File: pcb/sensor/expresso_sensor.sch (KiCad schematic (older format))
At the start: 13 parts, among them P1 CONN_2, P2 CONN_2, U1 TAOS_TSL1406R, U2 TAOS_TSL1406R, U3 TAOS_TSL1406R, U4 TAOS_TSL1406R, U5 TAOS_TSL1406R, U6 MAPLE_MINI

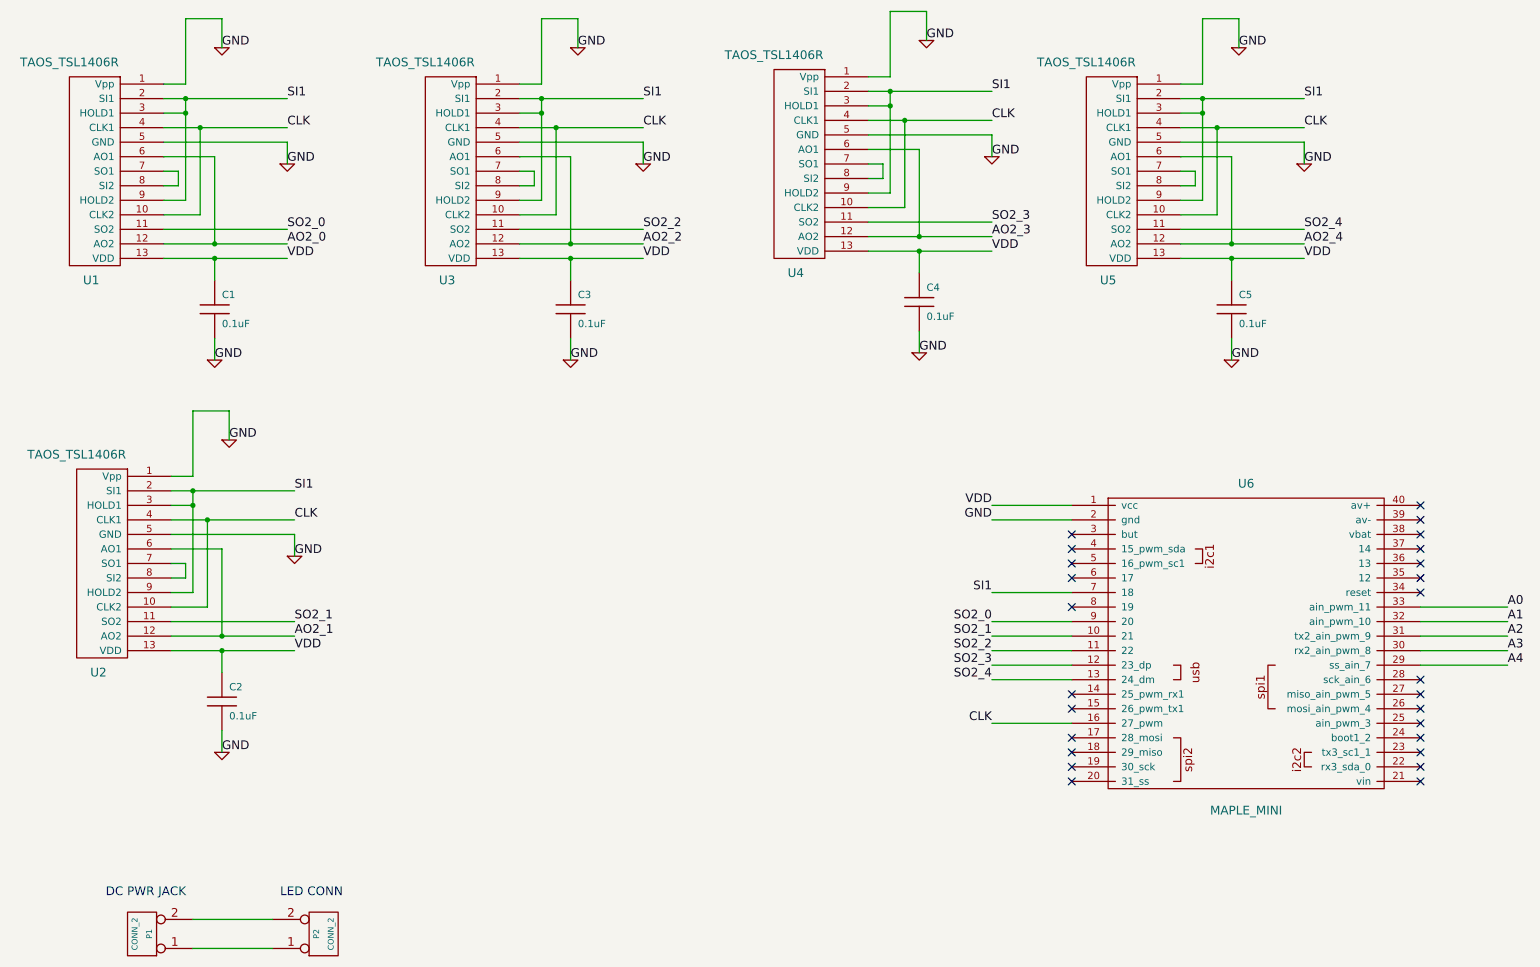
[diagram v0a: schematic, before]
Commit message: Major refactoring of the code for the enclosure.  Finished layout of the PCBs
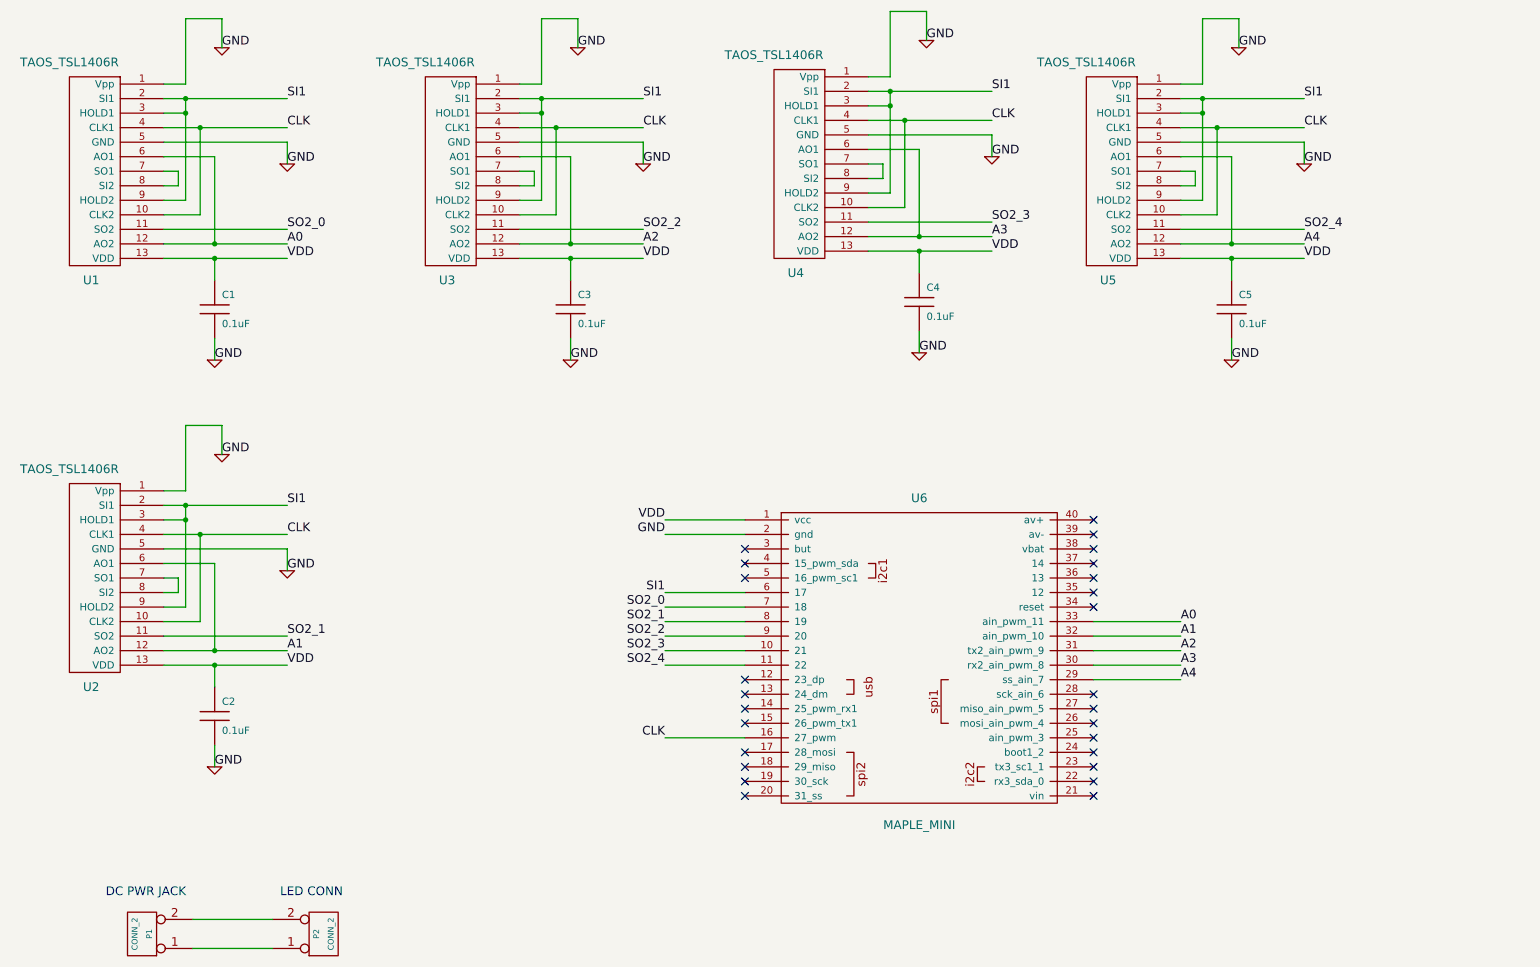
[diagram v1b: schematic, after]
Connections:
- net AO2_0 is gone; now on net A0: U1.12 (AO2), U1.6 (AO1)
- net AO2_1 is gone; now on net A1: U2.12 (AO2), U2.6 (AO1)
- net AO2_2 is gone; now on net A2: U3.12 (AO2), U3.6 (AO1)
- net AO2_3 is gone; now on net A3: U4.12 (AO2), U4.6 (AO1)
- net AO2_4 is gone; now on net A4: U5.12 (AO2), U5.6 (AO1)
- net SI1: now also U6.6 (17); no longer U6.7 (18)
- net SO2_0: now also U6.7 (18); no longer U6.9 (20)
- net SO2_1: now also U6.8 (19); no longer U6.10 (21)
- net SO2_2: now also U6.9 (20); no longer U6.11 (22)
- net SO2_3: now also U6.10 (21); no longer U6.12 (23_dp)
- net SO2_4: now also U6.11 (22); no longer U6.13 (24_dm)
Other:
- moved on the sheet: U6

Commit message: generated gerbers and finalized BOM
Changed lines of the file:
@@
-EESchema Schematic File Version 2  date Mon 17 Sep 2012 09:35:10 AM PDT
+EESchema Schematic File Version 2  date Fri 21 Sep 2012 01:45:22 PM PDT
 LIBS:power
 LIBS:device
@@
 $EndComp
 $Comp
-L GND #PWR?
+L GND #PWR01
 U 1 1 50575057
 P 2100 5750
-F 0 "#PWR?" H 2100 5750 30  0001 C CNN
+F 0 "#PWR01" H 2100 5750 30  0001 C CNN
 F 1 "GND" H 2100 5680 30  0001 C CNN
 	1    2100 5750
@@
 VDD
 $Comp
-L GND #PWR?
+L GND #PWR02
 U 1 1 50575056
 P 2150 3600
-F 0 "#PWR?" H 2150 3600 30  0001 C CNN
+F 0 "#PWR02" H 2150 3600 30  0001 C CNN
 F 1 "GND" H 2150 3530 30  0001 C CNN
 	1    2150 3600
@@
 GND
 $Comp
-L GND #PWR?
+L GND #PWR03
 U 1 1 50575055
 P 2600 4400
-F 0 "#PWR?" H 2600 4400 30  0001 C CNN
+F 0 "#PWR03" H 2600 4400 30  0001 C CNN
 F 1 "GND" H 2600 4330 30  0001 C CNN
 	1    2600 4400
@@
 Connection ~ 2100 5050
 Wire Wire Line
-	2100 5050 2100 5200
-Wire Wire Line
-	2000 4150 1750 4150
-Wire Wire Line
-	2600 4150 2000 4150
-Wire Wire Line
-	2100 4950 2600 4950
-Wire Wire Line
-	1750 4950 2100 4950
-Wire Wire Line
-	2100 4350 1750 4350
+	2100 5200 2100 5050
+Wire Wire Line
+	1750 4150 2600 4150
+Wire Wire Line
+	2600 4950 1750 4950
+Wire Wire Line
+	1750 4350 2100 4350
 Connection ~ 2000 4150
 Wire Wire Line
-	2000 4750 2000 4150
-Wire Wire Line
-	1750 4750 2000 4750
+	2000 4150 2000 4750
+Wire Wire Line
+	2000 4750 1750 4750
 Connection ~ 1900 4050
 Wire Wire Line
-	1900 4050 1900 3950
-Wire Wire Line
-	1900 4650 1900 4050
-Wire Wire Line
-	1750 4650 1900 4650
-Wire Wire Line
-	2150 3400 2150 3600
-Wire Wire Line
-	1900 3400 2150 3400
-Wire Wire Line
-	1900 3850 1900 3400
-Wire Wire Line
-	1750 3850 1900 3850
-Wire Wire Line
-	2100 5050 1750 5050
-Wire Wire Line
-	2600 5050 2100 5050
+	1900 3950 1900 4650
+Wire Wire Line
+	1900 4650 1750 4650
+Wire Wire Line
+	2150 3600 2150 3400
+Wire Wire Line
+	2150 3400 1900 3400
+Wire Wire Line
+	1900 3400 1900 3850
+Wire Wire Line
+	1900 3850 1750 3850
+Wire Wire Line
+	1750 5050 2600 5050
 Wire Wire Line
 	1900 4050 1750 4050
 Connection ~ 1900 3950
 Wire Wire Line
-	2600 4250 1750 4250
-Wire Wire Line
-	2600 4400 2600 4250
-Wire Wire Line
-	1900 3950 1750 3950
-Wire Wire Line
-	2600 3950 1900 3950
-Wire Wire Line
-	2100 4950 2100 4350
+	1750 4250 2600 4250
+Wire Wire Line
+	2600 4250 2600 4400
+Wire Wire Line
+	1750 3950 2600 3950
+Wire Wire Line
+	2100 4350 2100 4950
 Connection ~ 2100 4950
 Wire Wire Line
 	2100 5600 2100 5750
 Wire Wire Line
-	1850 4450 1750 4450
-Wire Wire Line
-	1850 4550 1850 4450
-Wire Wire Line
-	1750 4550 1850 4550
+	1750 4450 1850 4450
+Wire Wire Line
+	1850 4450 1850 4550
+Wire Wire Line
+	1850 4550 1750 4550
 Text Label 5200 5050 2    60   ~ 0
 SO2_4
@@
 Connection ~ 9100 2250
 Wire Wire Line
-	9100 2250 9100 2400
-Wire Wire Line
-	9600 1350 9000 1350
-Wire Wire Line
-	9000 1350 8750 1350
-Wire Wire Line
-	8750 2150 9100 2150
-Wire Wire Line
-	9100 2150 9600 2150
+	9100 2400 9100 2250
+Wire Wire Line
+	9600 1350 8750 1350
+Wire Wire Line
+	8750 2150 9600 2150
 Wire Wire Line
 	8750 1550 9100 1550
@@
 Connection ~ 8900 1250
 Wire Wire Line
-	8900 1150 8900 1250
-Wire Wire Line
-	8900 1250 8900 1850
+	8900 1150 8900 1850
 Wire Wire Line
 	8900 1850 8750 1850
@@
 	8900 1050 8750 1050
 Wire Wire Line
-	9600 2250 9100 2250
-Wire Wire Line
-	9100 2250 8750 2250
+	9600 2250 8750 2250
 Wire Wire Line
 	8900 1250 8750 1250
@@
 	9600 1450 9600 1600
 Wire Wire Line
-	9600 1150 8900 1150
-Wire Wire Line
-	8900 1150 8750 1150
+	9600 1150 8750 1150
 Wire Wire Line
 	9100 1550 9100 2150
@@
 Connection ~ 4550 2250
 Wire Wire Line
-	4550 2250 4550 2400
-Wire Wire Line
-	5050 1350 4450 1350
-Wire Wire Line
-	4450 1350 4200 1350
-Wire Wire Line
-	4200 2150 4550 2150
-Wire Wire Line
-	4550 2150 5050 2150
+	4550 2400 4550 2250
+Wire Wire Line
+	5050 1350 4200 1350
+Wire Wire Line
+	4200 2150 5050 2150
 Wire Wire Line
 	4200 1550 4550 1550
@@
 Connection ~ 4350 1250
 Wire Wire Line
-	4350 1150 4350 1250
-Wire Wire Line
-	4350 1250 4350 1850
+	4350 1150 4350 1850
 Wire Wire Line
 	4350 1850 4200 1850
@@
 	4350 1050 4200 1050
 Wire Wire Line
-	5050 2250 4550 2250
-Wire Wire Line
-	4550 2250 4200 2250
+	5050 2250 4200 2250
 Wire Wire Line
 	4350 1250 4200 1250
@@
 	5050 1450 5050 1600
 Wire Wire Line
-	5050 1150 4350 1150
-Wire Wire Line
-	4350 1150 4200 1150
+	5050 1150 4200 1150
 Wire Wire Line
 	4550 1550 4550 2150
@@
 	6950 2100 6950 1500
 Wire Wire Line
-	7450 1100 6750 1100
-Wire Wire Line
-	6750 1100 6600 1100
+	7450 1100 6600 1100
 Wire Wire Line
 	7450 1550 7450 1400
@@
 Connection ~ 6750 1100
 Wire Wire Line
-	6750 1200 6600 1200
-Wire Wire Line
-	7450 2200 6950 2200
-Wire Wire Line
-	6950 2200 6600 2200
+	6600 1200 6750 1200
+Wire Wire Line
+	7450 2200 6600 2200
 Wire Wire Line
 	6600 1000 6750 1000
@@
 	6600 1800 6750 1800
 Wire Wire Line
-	6750 1800 6750 1200
-Wire Wire Line
-	6750 1200 6750 1100
+	6750 1800 6750 1100
 Connection ~ 6750 1200
 Wire Wire Line
@@
 	6950 1500 6600 1500
 Wire Wire Line
-	6600 2100 6950 2100
-Wire Wire Line
-	6950 2100 7450 2100
-Wire Wire Line
-	7450 1300 6850 1300
-Wire Wire Line
-	6850 1300 6600 1300
+	6600 2100 7450 2100
+Wire Wire Line
+	7450 1300 6600 1300
 Wire Wire Line
 	6950 2200 6950 2350
@@
 	2100 2150 2100 1550
 Wire Wire Line
-	2600 1150 1900 1150
-Wire Wire Line
-	1900 1150 1750 1150
+	2600 1150 1750 1150
 Wire Wire Line
 	2600 1600 2600 1450
@@
 Connection ~ 1900 1150
 Wire Wire Line
-	1900 1250 1750 1250
+	1750 1250 1900 1250
 Wire Wire Line
 	5750 4550 5200 4550
@@
 	5750 4050 5200 4050
 Wire Wire Line
-	2600 2250 2100 2250
-Wire Wire Line
-	2100 2250 1750 2250
+	2600 2250 1750 2250
 Wire Wire Line
 	2500 6800 1950 6800
@@
 	1750 1850 1900 1850
 Wire Wire Line
-	1900 1850 1900 1250
-Wire Wire Line
-	1900 1250 1900 1150
+	1900 1850 1900 1150
 Connection ~ 1900 1250
 Wire Wire Line
@@
 	2100 1550 1750 1550
 Wire Wire Line
-	1750 2150 2100 2150
-Wire Wire Line
-	2100 2150 2600 2150
-Wire Wire Line
-	2600 1350 2000 1350
-Wire Wire Line
-	2000 1350 1750 1350
+	1750 2150 2600 2150
+Wire Wire Line
+	2600 1350 1750 1350
 Wire Wire Line
 	2100 2250 2100 2400
@@
 $EndComp
 $Comp
-L GND #PWR01
+L GND #PWR04
 U 1 1 4F36C830
 P 9100 2950
-F 0 "#PWR01" H 9100 2950 30  0001 C CNN
+F 0 "#PWR04" H 9100 2950 30  0001 C CNN
 F 1 "GND" H 9100 2880 30  0001 C CNN
 	1    9100 2950
@@
 VDD
 $Comp
-L GND #PWR02
+L GND #PWR05
 U 1 1 4F36C82F
 P 9150 800
-F 0 "#PWR02" H 9150 800 30  0001 C CNN
+F 0 "#PWR05" H 9150 800 30  0001 C CNN
 F 1 "GND" H 9150 730 30  0001 C CNN
 	1    9150 800
@@
 GND
 $Comp
-L GND #PWR03
+L GND #PWR06
 U 1 1 4F36C82E
 P 9600 1600
-F 0 "#PWR03" H 9600 1600 30  0001 C CNN
+F 0 "#PWR06" H 9600 1600 30  0001 C CNN
 F 1 "GND" H 9600 1530 30  0001 C CNN
 	1    9600 1600
@@
 $EndComp
 $Comp
-L GND #PWR04
+L GND #PWR07
 U 1 1 4F36C825
 P 4550 2950
-F 0 "#PWR04" H 4550 2950 30  0001 C CNN
+F 0 "#PWR07" H 4550 2950 30  0001 C CNN
 F 1 "GND" H 4550 2880 30  0001 C CNN
 	1    4550 2950
@@
 VDD
 $Comp
-L GND #PWR05
+L GND #PWR08
 U 1 1 4F36C824
 P 4600 800
-F 0 "#PWR05" H 4600 800 30  0001 C CNN
+F 0 "#PWR08" H 4600 800 30  0001 C CNN
 F 1 "GND" H 4600 730 30  0001 C CNN
 	1    4600 800
@@
 GND
 $Comp
-L GND #PWR06
+L GND #PWR09
 U 1 1 4F36C823
 P 5050 1600
-F 0 "#PWR06" H 5050 1600 30  0001 C CNN
+F 0 "#PWR09" H 5050 1600 30  0001 C CNN
 F 1 "GND" H 5050 1530 30  0001 C CNN
 	1    5050 1600
@@
 GND
 $Comp
-L GND #PWR07
+L GND #PWR010
 U 1 1 4F36C822
 P 7450 1550
-F 0 "#PWR07" H 7450 1550 30  0001 C CNN
+F 0 "#PWR010" H 7450 1550 30  0001 C CNN
 F 1 "GND" H 7450 1480 30  0001 C CNN
 	1    7450 1550
@@
 GND
 $Comp
-L GND #PWR08
+L GND #PWR011
 U 1 1 4F36C821
 P 7000 750
-F 0 "#PWR08" H 7000 750 30  0001 C CNN
+F 0 "#PWR011" H 7000 750 30  0001 C CNN
 F 1 "GND" H 7000 680 30  0001 C CNN
 	1    7000 750
@@
 GND
 $Comp
-L GND #PWR09
+L GND #PWR012
 U 1 1 4F36C820
 P 6950 2900
-F 0 "#PWR09" H 6950 2900 30  0001 C CNN
+F 0 "#PWR012" H 6950 2900 30  0001 C CNN
 F 1 "GND" H 6950 2830 30  0001 C CNN
 	1    6950 2900

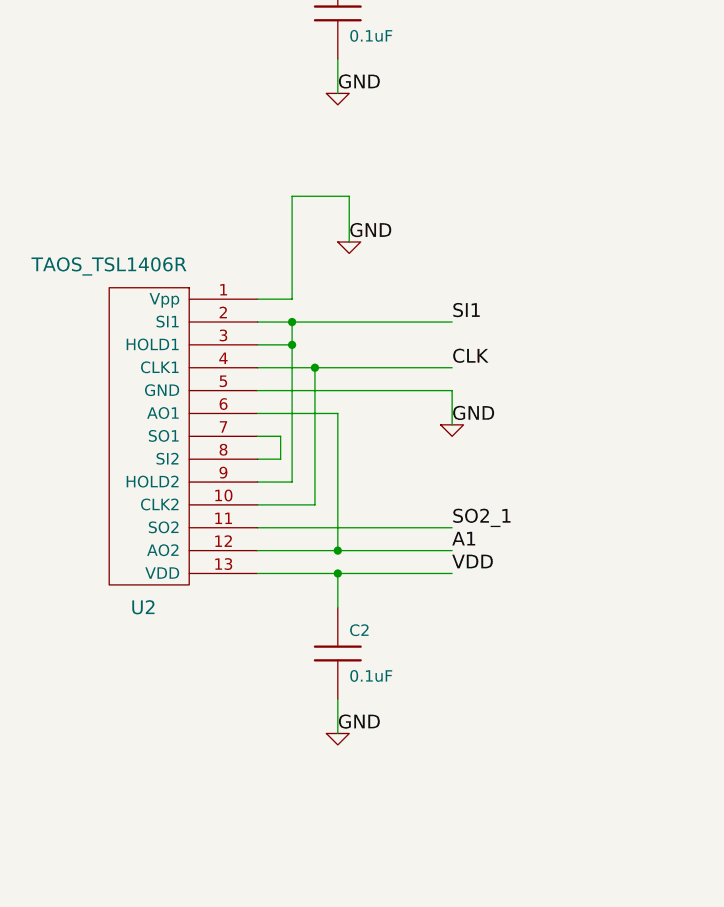
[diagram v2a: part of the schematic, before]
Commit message: Redesigned sensor pcb, and modified enclosure accordingly.
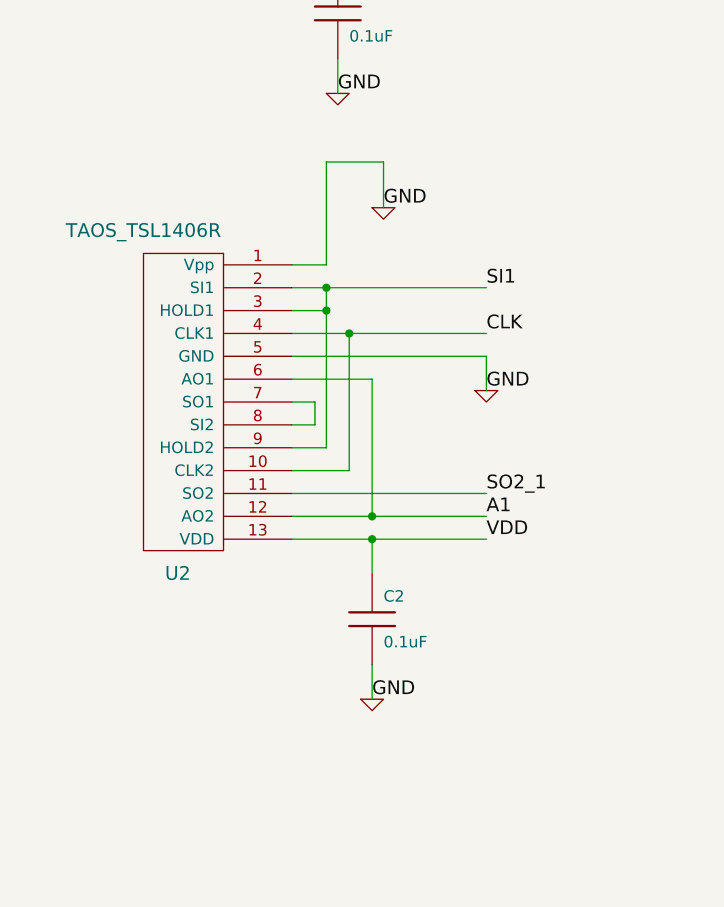
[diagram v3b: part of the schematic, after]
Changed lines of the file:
@@
-EESchema Schematic File Version 2  date Fri 21 Sep 2012 01:45:22 PM PDT
+EESchema Schematic File Version 2  date Thu 11 Oct 2012 06:36:20 PM PDT
 LIBS:power
 LIBS:device
@@
 Sheet 1 1
 Title ""
-Date "17 sep 2012"
+Date "12 oct 2012"
 Rev ""
 Comp ""
@@
 Comment4 ""
 $EndDescr
-NoConn ~ 5750 5250
-NoConn ~ 5750 5150
 $Comp
 L TAOS_TSL1406R U2
-U 1 1 50575059
-P 1450 4450
-F 0 "U2" H 1650 3700 60  0000 C CNN
-F 1 "TAOS_TSL1406R" H 1800 5200 60  0000 C CNN
-	1    1450 4450
+U 1 1 5077711F
+P 1600 4300
+F 0 "U2" H 1800 3550 60  0000 C CNN
+F 1 "TAOS_TSL1406R" H 1950 5050 60  0000 C CNN
+	1    1600 4300
 	-1   0    0    -1
 $EndComp
 $Comp
 L C C2
-U 1 1 50575058
-P 2100 5400
-F 0 "C2" H 2150 5500 50  0000 L CNN
-F 1 "0.1uF" H 2150 5300 50  0000 L CNN
-	1    2100 5400
+U 1 1 5077711E
+P 2250 5250
+F 0 "C2" H 2300 5350 50  0000 L CNN
+F 1 "0.1uF" H 2300 5150 50  0000 L CNN
+	1    2250 5250
 	1    0    0    -1
 $EndComp
 $Comp
-L GND #PWR01
-U 1 1 50575057
-P 2100 5750
-F 0 "#PWR01" H 2100 5750 30  0001 C CNN
-F 1 "GND" H 2100 5680 30  0001 C CNN
-	1    2100 5750
+L GND #PWR?
+U 1 1 5077711D
+P 2250 5600
+F 0 "#PWR?" H 2250 5600 30  0001 C CNN
+F 1 "GND" H 2250 5530 30  0001 C CNN
+	1    2250 5600
 	1    0    0    -1
 $EndComp
-Text Label 2100 5750 0    60   ~ 0
+Text Label 2250 5600 0    60   ~ 0
 GND
-Text Label 2600 5050 0    60   ~ 0
+Text Label 2750 4900 0    60   ~ 0
 VDD
 $Comp
-L GND #PWR02
-U 1 1 50575056
-P 2150 3600
-F 0 "#PWR02" H 2150 3600 30  0001 C CNN
-F 1 "GND" H 2150 3530 30  0001 C CNN
-	1    2150 3600
+L GND #PWR?
+U 1 1 5077711C
+P 2300 3450
+F 0 "#PWR?" H 2300 3450 30  0001 C CNN
+F 1 "GND" H 2300 3380 30  0001 C CNN
+	1    2300 3450
 	1    0    0    -1
 $EndComp
-Text Label 2150 3600 0    60   ~ 0
+Text Label 2300 3450 0    60   ~ 0
 GND
 $Comp
-L GND #PWR03
-U 1 1 50575055
-P 2600 4400
-F 0 "#PWR03" H 2600 4400 30  0001 C CNN
-F 1 "GND" H 2600 4330 30  0001 C CNN
-	1    2600 4400
+L GND #PWR?
+U 1 1 5077711B
+P 2750 4250
+F 0 "#PWR?" H 2750 4250 30  0001 C CNN
+F 1 "GND" H 2750 4180 30  0001 C CNN
+	1    2750 4250
 	1    0    0    -1
 $EndComp
-Text Label 2600 4400 0    60   ~ 0
+Text Label 2750 4250 0    60   ~ 0
 GND
-Text Label 2600 3950 0    60   ~ 0
+Text Label 2750 3800 0    60   ~ 0
 SI1
-Text Label 2600 4150 0    60   ~ 0
+Text Label 2750 4000 0    60   ~ 0
 CLK
-Text Label 2600 4850 0    60   ~ 0
+Text Label 2750 4700 0    60   ~ 0
 SO2_1
-Text Label 2600 4950 0    60   ~ 0
+Text Label 2750 4800 0    60   ~ 0
 A1
 Wire Wire Line
-	1750 4850 2600 4850
-Connection ~ 2100 5050
+	1900 4700 2750 4700
+Connection ~ 2250 4900
 Wire Wire Line
-	2100 5200 2100 5050
+	2250 4900 2250 5050
 Wire Wire Line
-	1750 4150 2600 4150
+	2750 4000 1900 4000
 Wire Wire Line
-	2600 4950 1750 4950
+	1900 4800 2750 4800
 Wire Wire Line
-	1750 4350 2100 4350
-Connection ~ 2000 4150
+	2250 4200 1900 4200
+Connection ~ 2150 4000
 Wire Wire Line
-	2000 4150 2000 4750
+	2150 4600 2150 4000
 Wire Wire Line
-	2000 4750 1750 4750
-Connection ~ 1900 4050
+	1900 4600 2150 4600
+Connection ~ 2050 3900
 Wire Wire Line
-	1900 3950 1900 4650
+	2050 4500 2050 3800
 Wire Wire Line
-	1900 4650 1750 4650
+	1900 4500 2050 4500
 Wire Wire Line
-	2150 3600 2150 3400
+	2300 3250 2300 3450
 Wire Wire Line
-	2150 3400 1900 3400
+	2050 3250 2300 3250
 Wire Wire Line
-	1900 3400 1900 3850
+	2050 3700 2050 3250
 Wire Wire Line
-	1900 3850 1750 3850
+	1900 3700 2050 3700
 Wire Wire Line
-	1750 5050 2600 5050
+	2750 4900 1900 4900
 Wire Wire Line
-	1900 4050 1750 4050
-Connection ~ 1900 3950
+	1900 3900 2050 3900
+Connection ~ 2050 3800
 Wire Wire Line
-	1750 4250 2600 4250
+	2750 4100 1900 4100
 Wire Wire Line
-	2600 4250 2600 4400
+	2750 4250 2750 4100
 Wire Wire Line
-	1750 3950 2600 3950
+	2750 3800 1900 3800
 Wire Wire Line
-	2100 4350 2100 4950
-Connection ~ 2100 4950
+	2250 4800 2250 4200
+Connection ~ 2250 4800
 Wire Wire Line
-	2100 5600 2100 5750
+	2250 5450 2250 5600
 Wire Wire Line
-	1750 4450 1850 4450
+	2000 4300 1900 4300
 Wire Wire Line
-	1850 4450 1850 4550
+	2000 4400 2000 4300
 Wire Wire Line
-	1850 4550 1750 4550
+	1900 4400 2000 4400
+NoConn ~ 5750 5250
+NoConn ~ 5750 5150
 Text Label 5200 5050 2    60   ~ 0
 SO2_4
